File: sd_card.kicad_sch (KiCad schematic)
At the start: 3 parts

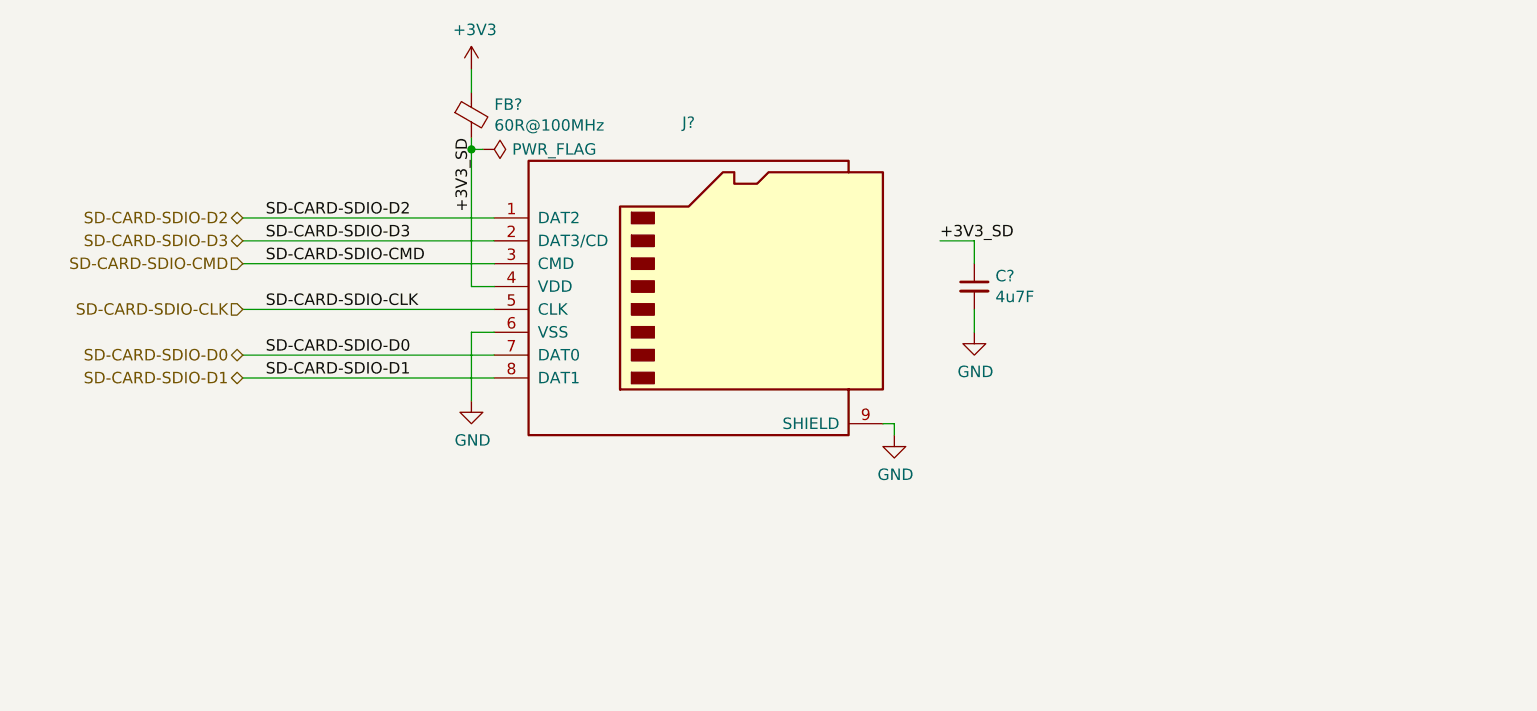
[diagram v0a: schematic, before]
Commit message: Refactor the mainboard
- Use smaller STM
- Use MPU-9250 as a motion sensor
- Connect some peripherals to the MCU
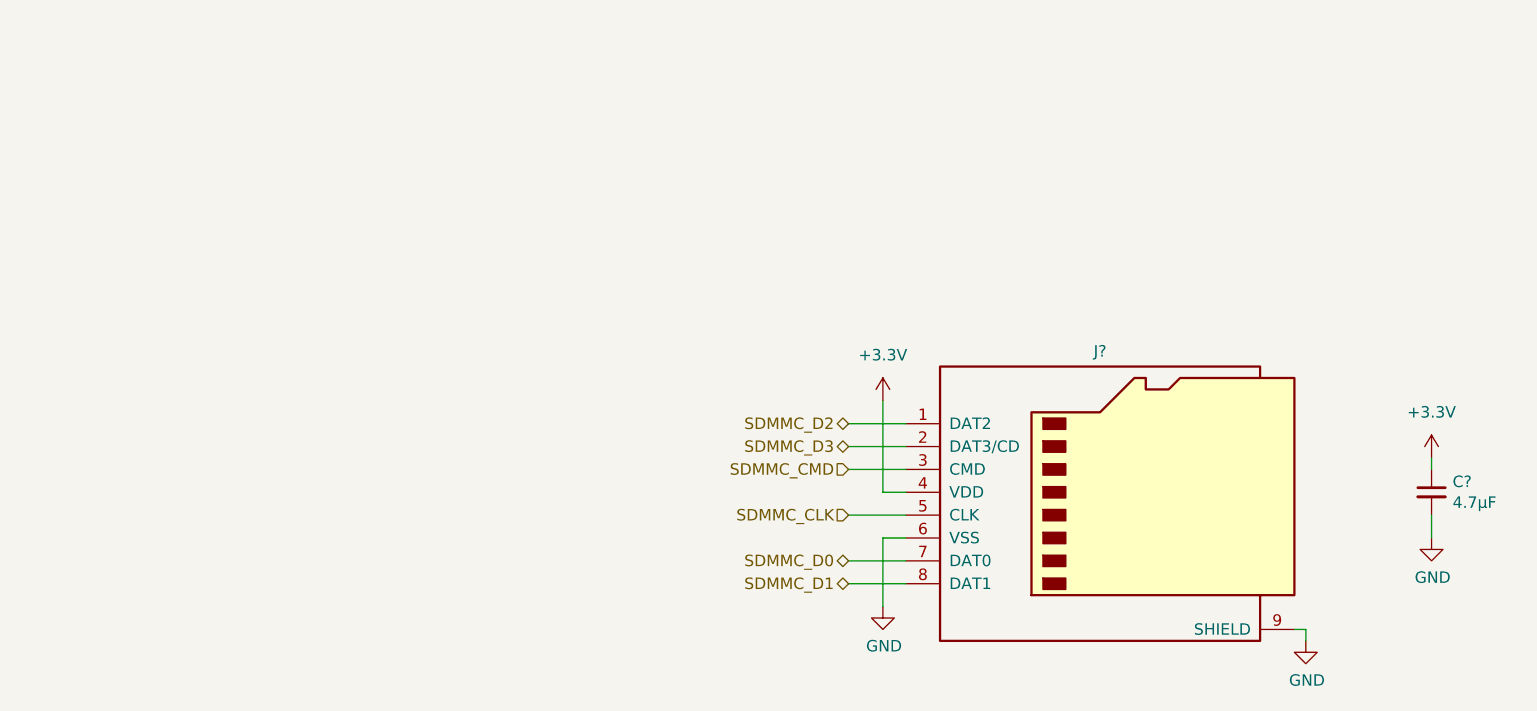
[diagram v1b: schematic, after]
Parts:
- removed FB?: 60R@100MHz, Inductor_SMD:L_0603_1608Metric, symbol Device:Ferrite_Bead_Small
- C?: value 4u7F -> 4.7μF
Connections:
- net +3V3_SD renamed +3.3V
- net SD-CARD-SDIO-CLK renamed SDMMC_CLK
- net SD-CARD-SDIO-CMD renamed SDMMC_CMD
- net SD-CARD-SDIO-D0 renamed SDMMC_D0
- net SD-CARD-SDIO-D1 renamed SDMMC_D1
- net SD-CARD-SDIO-D2 renamed SDMMC_D2
- net SD-CARD-SDIO-D3 renamed SDMMC_D3
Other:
- moved on the sheet: C?, J?

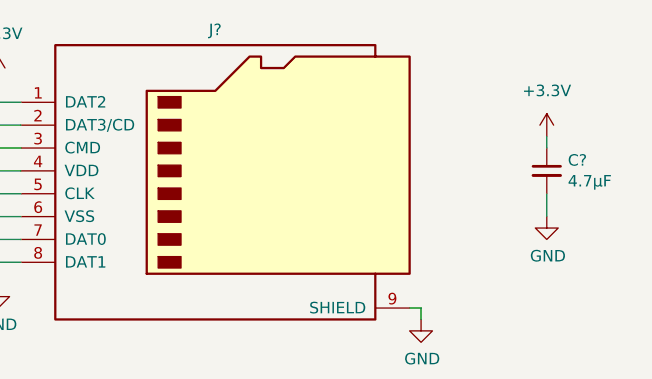
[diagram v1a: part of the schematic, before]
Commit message: Connect sensors to the MCU
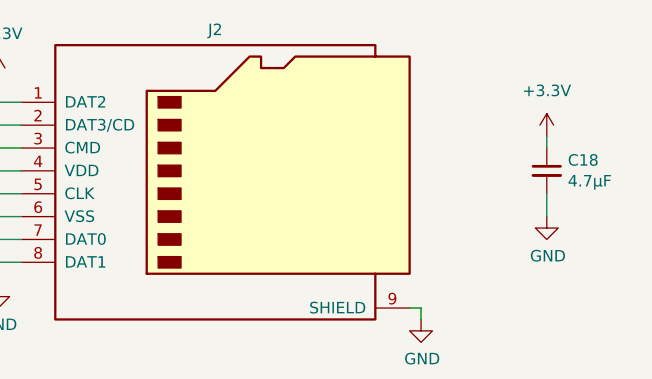
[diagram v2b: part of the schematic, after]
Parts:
- gave numbers to parts that had none: 2
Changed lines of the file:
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@@
 (kicad_sch (version 20211123) (generator eeschema)
   (paper "A4")
+  (title_block
+    (date "2022-12-16")
+    (rev "0.1.0")
+  )
   (wire (pts (xy 186.69 118.11) (xy 185.42 118.11))
     (stroke (width 0) (type default) (color 0 0 0 0))
@@
   (symbol (lib_id "Connector:Micro_SD_Card") (at 165.1 102.87 0) (unit 1)
     (in_bom yes) (on_board yes)
-    (property "Reference" "J?" (id 0) (at 163.83 87.1982 0))
+    (property "Reference" "J2" (id 0) (at 163.83 87.1982 0))
     (property "Value" "Micro_SD_Card" (id 1) (at 163.83 86.9696 0)
       (effects (font (size 1.27 1.27)) hide)
@@
   (symbol (lib_id "Device:C_Small") (at 200.66 102.87 0) (unit 1)
     (in_bom yes) (on_board yes)
-    (property "Reference" "C?" (id 0) (at 202.9968 101.7016 0)
+    (property "Reference" "C18" (id 0) (at 202.9968 101.7016 0)
       (effects (font (size 1.27 1.27)) (justify left))
     )
@@
   (symbol (lib_id "power:GND") (at 200.66 107.95 0) (unit 1)
     (in_bom yes) (on_board yes)
-    (property "Reference" "#PWR?" (id 0) (at 200.66 114.3 0)
+    (property "Reference" "#PWR0135" (id 0) (at 200.66 114.3 0)
       (effects (font (size 1.27 1.27)) hide)
     )
@@
   (symbol (lib_id "power:+3.3V") (at 200.66 99.06 0) (unit 1)
     (in_bom yes) (on_board yes) (fields_autoplaced)
-    (property "Reference" "#PWR?" (id 0) (at 200.66 102.87 0)
+    (property "Reference" "#PWR0134" (id 0) (at 200.66 102.87 0)
       (effects (font (size 1.27 1.27)) hide)
     )
@@
   (symbol (lib_id "power:+3.3V") (at 139.7 92.71 0) (unit 1)
     (in_bom yes) (on_board yes) (fields_autoplaced)
-    (property "Reference" "#PWR?" (id 0) (at 139.7 96.52 0)
+    (property "Reference" "#PWR0137" (id 0) (at 139.7 96.52 0)
       (effects (font (size 1.27 1.27)) hide)
     )
@@
   (symbol (lib_id "power:GND") (at 139.7 115.57 0) (unit 1)
     (in_bom yes) (on_board yes)
-    (property "Reference" "#PWR?" (id 0) (at 139.7 121.92 0)
+    (property "Reference" "#PWR0133" (id 0) (at 139.7 121.92 0)
       (effects (font (size 1.27 1.27)) hide)
     )
@@
   (symbol (lib_id "power:GND") (at 186.69 119.38 0) (unit 1)
     (in_bom yes) (on_board yes)
-    (property "Reference" "#PWR?" (id 0) (at 186.69 125.73 0)
+    (property "Reference" "#PWR0136" (id 0) (at 186.69 125.73 0)
       (effects (font (size 1.27 1.27)) hide)
     )

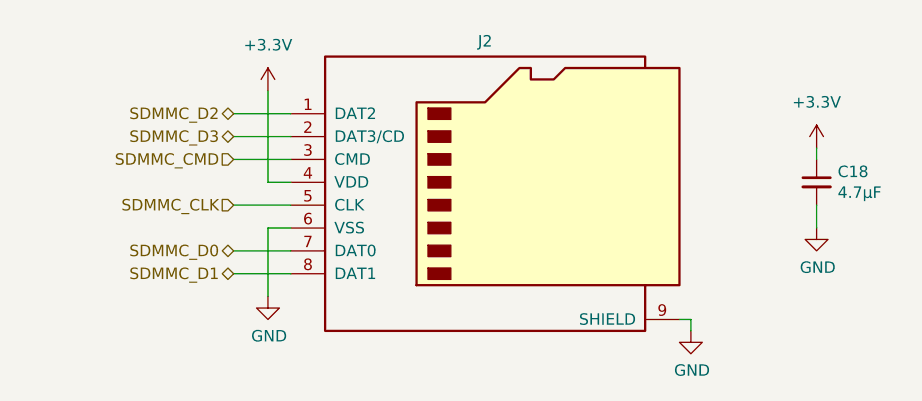
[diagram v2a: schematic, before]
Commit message: Improve the power section:
- add ADC circuit to measure battery level
- add 5V LDO regulator
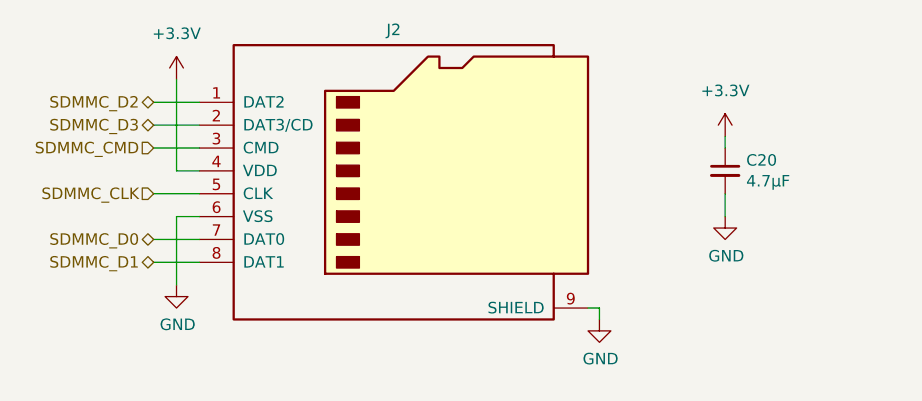
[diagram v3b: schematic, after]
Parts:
- renumbered C18 to C20
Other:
- title: (none) -> SD Card
- moved on the sheet: C20, J2
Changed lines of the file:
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@@
   (paper "A4")
   (title_block
-    (date "2022-12-16")
+    (title "SD Card")
+    (date "2022-12-17")
     (rev "0.1.0")
   )
-  (wire (pts (xy 186.69 118.11) (xy 185.42 118.11))
+  (wire (pts (xy 176.53 116.84) (xy 175.26 116.84))
     (stroke (width 0) (type default) (color 0 0 0 0))
   )
-  (wire (pts (xy 135.89 95.25) (xy 142.24 95.25))
+  (wire (pts (xy 127 93.98) (xy 132.08 93.98))
     (stroke (width 0) (type default) (color 0 0 0 0))
   )
-  (wire (pts (xy 142.24 113.03) (xy 135.89 113.03))
+  (wire (pts (xy 132.08 111.76) (xy 127 111.76))
     (stroke (width 0) (type default) (color 0 0 0 0))
   )
-  (wire (pts (xy 135.89 105.41) (xy 142.24 105.41))
+  (wire (pts (xy 127 104.14) (xy 132.08 104.14))
     (stroke (width 0) (type default) (color 0 0 0 0))
   )
-  (wire (pts (xy 139.7 107.95) (xy 142.24 107.95))
+  (wire (pts (xy 129.54 106.68) (xy 132.08 106.68))
     (stroke (width 0) (type default) (color 0 0 0 0))
   )
-  (wire (pts (xy 200.66 105.41) (xy 200.66 107.95))
+  (wire (pts (xy 190.5 104.14) (xy 190.5 106.68))
     (stroke (width 0) (type default) (color 0 0 0 0))
   )
-  (wire (pts (xy 186.69 119.38) (xy 186.69 118.11))
+  (wire (pts (xy 176.53 118.11) (xy 176.53 116.84))
     (stroke (width 0) (type default) (color 0 0 0 0))
   )
-  (wire (pts (xy 135.89 97.79) (xy 142.24 97.79))
+  (wire (pts (xy 127 96.52) (xy 132.08 96.52))
     (stroke (width 0) (type default) (color 0 0 0 0))
   )
-  (wire (pts (xy 135.89 110.49) (xy 142.24 110.49))
+  (wire (pts (xy 127 109.22) (xy 132.08 109.22))
     (stroke (width 0) (type default) (color 0 0 0 0))
   )
-  (wire (pts (xy 200.66 99.06) (xy 200.66 100.33))
+  (wire (pts (xy 190.5 97.79) (xy 190.5 99.06))
     (stroke (width 0) (type default) (color 0 0 0 0))
   )
-  (wire (pts (xy 142.24 102.87) (xy 139.7 102.87))
+  (wire (pts (xy 132.08 101.6) (xy 129.54 101.6))
     (stroke (width 0) (type default) (color 0 0 0 0))
   )
-  (wire (pts (xy 139.7 115.57) (xy 139.7 107.95))
+  (wire (pts (xy 129.54 114.3) (xy 129.54 106.68))
     (stroke (width 0) (type default) (color 0 0 0 0))
   )
-  (wire (pts (xy 139.7 92.71) (xy 139.7 102.87))
+  (wire (pts (xy 129.54 91.44) (xy 129.54 101.6))
     (stroke (width 0) (type default) (color 0 0 0 0))
   )
-  (wire (pts (xy 135.89 100.33) (xy 142.24 100.33))
+  (wire (pts (xy 127 99.06) (xy 132.08 99.06))
     (stroke (width 0) (type default) (color 0 0 0 0))
   )
-  (hierarchical_label "SDMMC_D3" (shape bidirectional) (at 135.89 97.79 180)
+  (hierarchical_label "SDMMC_D3" (shape bidirectional) (at 127 96.52 180)
     (effects (font (size 1.27 1.27)) (justify right))
   )
-  (hierarchical_label "SDMMC_D1" (shape bidirectional) (at 135.89 113.03 180)
+  (hierarchical_label "SDMMC_D1" (shape bidirectional) (at 127 111.76 180)
     (effects (font (size 1.27 1.27)) (justify right))
   )
-  (hierarchical_label "SDMMC_D2" (shape bidirectional) (at 135.89 95.25 180)
+  (hierarchical_label "SDMMC_D2" (shape bidirectional) (at 127 93.98 180)
     (effects (font (size 1.27 1.27)) (justify right))
   )
-  (hierarchical_label "SDMMC_D0" (shape bidirectional) (at 135.89 110.49 180)
+  (hierarchical_label "SDMMC_D0" (shape bidirectional) (at 127 109.22 180)
     (effects (font (size 1.27 1.27)) (justify right))
   )
-  (hierarchical_label "SDMMC_CLK" (shape input) (at 135.89 105.41 180)
+  (hierarchical_label "SDMMC_CLK" (shape input) (at 127 104.14 180)
     (effects (font (size 1.27 1.27)) (justify right))
   )
-  (hierarchical_label "SDMMC_CMD" (shape input) (at 135.89 100.33 180)
+  (hierarchical_label "SDMMC_CMD" (shape input) (at 127 99.06 180)
     (effects (font (size 1.27 1.27)) (justify right))
   )
-  (symbol (lib_id "Connector:Micro_SD_Card") (at 165.1 102.87 0) (unit 1)
+  (symbol (lib_id "Connector:Micro_SD_Card") (at 154.94 101.6 0) (unit 1)
     (in_bom yes) (on_board yes)
-    (property "Reference" "J2" (id 0) (at 163.83 87.1982 0))
-    (property "Value" "Micro_SD_Card" (id 1) (at 163.83 86.9696 0)
+    (property "Reference" "J2" (id 0) (at 153.67 85.9282 0))
+    (property "Value" "Micro_SD_Card" (id 1) (at 153.67 85.6996 0)
       (effects (font (size 1.27 1.27)) hide)
     )
-    (property "Footprint" "PUTM_Kicad_FOOTPRINTS:112K-TAA0-RA1" (id 2) (at 194.31 95.25 0)
+    (property "Footprint" "PUTM_Kicad_FOOTPRINTS:112K-TAA0-RA1" (id 2) (at 184.15 93.98 0)
       (effects (font (size 1.27 1.27)) hide)
     )
-    (property "Datasheet" "https://www.tme.eu/Document/c3b9a7ded342d5553aff6a91c42e4fab/112K-TAA0-RA1.pdf" (id 3) (at 165.1 102.87 0)
+    (property "Datasheet" "https://www.tme.eu/Document/c3b9a7ded342d5553aff6a91c42e4fab/112K-TAA0-RA1.pdf" (id 3) (at 154.94 101.6 0)
       (effects (font (size 1.27 1.27)) hide)
     )
@@
     (pin "9")
   )
-  (symbol (lib_id "Device:C_Small") (at 200.66 102.87 0) (unit 1)
+  (symbol (lib_id "Device:C_Small") (at 190.5 101.6 0) (unit 1)
     (in_bom yes) (on_board yes)
-    (property "Reference" "C18" (id 0) (at 202.9968 101.7016 0)
+    (property "Reference" "C20" (id 0) (at 192.8368 100.4316 0)
       (effects (font (size 1.27 1.27)) (justify left))
     )
-    (property "Value" "4.7μF" (id 1) (at 202.9968 104.013 0)
+    (property "Value" "4.7μF" (id 1) (at 192.8368 102.743 0)
       (effects (font (size 1.27 1.27)) (justify left))
     )
-    (property "Footprint" "Capacitor_SMD:C_0603_1608Metric" (id 2) (at 200.66 102.87 0)
+    (property "Footprint" "Capacitor_SMD:C_0603_1608Metric" (id 2) (at 190.5 101.6 0)
       (effects (font (size 1.27 1.27)) hide)
     )
-    (property "Datasheet" "~" (id 3) (at 200.66 102.87 0)
+    (property "Datasheet" "~" (id 3) (at 190.5 101.6 0)
       (effects (font (size 1.27 1.27)) hide)
     )
-    (property "LCSC" "C19666" (id 4) (at 200.66 102.87 0)
+    (property "LCSC" "C19666" (id 4) (at 190.5 101.6 0)
       (effects (font (size 1.27 1.27)) hide)
     )
@@
     (pin "2")
   )
-  (symbol (lib_id "power:GND") (at 200.66 107.95 0) (unit 1)
+  (symbol (lib_id "power:GND") (at 190.5 106.68 0) (unit 1)
     (in_bom yes) (on_board yes)
-    (property "Reference" "#PWR0135" (id 0) (at 200.66 114.3 0)
+    (property "Reference" "#PWR040" (id 0) (at 190.5 113.03 0)
       (effects (font (size 1.27 1.27)) hide)
     )
-    (property "Value" "GND" (id 1) (at 200.787 112.3442 0))
-    (property "Footprint" "" (id 2) (at 200.66 107.95 0)
+    (property "Value" "GND" (id 1) (at 190.627 111.0742 0))
+    (property "Footprint" "" (id 2) (at 190.5 106.68 0)
       (effects (font (size 1.27 1.27)) hide)
     )
-    (property "Datasheet" "" (id 3) (at 200.66 107.95 0)
+    (property "Datasheet" "" (id 3) (at 190.5 106.68 0)
       (effects (font (size 1.27 1.27)) hide)
     )
     (pin "1")
   )
-  (symbol (lib_id "power:+3.3V") (at 200.66 99.06 0) (unit 1)
+  (symbol (lib_id "power:+3.3V") (at 190.5 97.79 0) (unit 1)
     (in_bom yes) (on_board yes) (fields_autoplaced)
-    (property "Reference" "#PWR0134" (id 0) (at 200.66 102.87 0)
+    (property "Reference" "#PWR039" (id 0) (at 190.5 101.6 0)
       (effects (font (size 1.27 1.27)) hide)
     )
-    (property "Value" "+3.3V" (id 1) (at 200.66 93.98 0))
-    (property "Footprint" "" (id 2) (at 200.66 99.06 0)
+    (property "Value" "+3.3V" (id 1) (at 190.5 92.71 0))
+    (property "Footprint" "" (id 2) (at 190.5 97.79 0)
       (effects (font (size 1.27 1.27)) hide)
     )
-    (property "Datasheet" "" (id 3) (at 200.66 99.06 0)
+    (property "Datasheet" "" (id 3) (at 190.5 97.79 0)
       (effects (font (size 1.27 1.27)) hide)
     )
     (pin "1")
   )
-  (symbol (lib_id "power:+3.3V") (at 139.7 92.71 0) (unit 1)
+  (symbol (lib_id "power:+3.3V") (at 129.54 91.44 0) (unit 1)
     (in_bom yes) (on_board yes) (fields_autoplaced)
-    (property "Reference" "#PWR0137" (id 0) (at 139.7 96.52 0)
+    (property "Reference" "#PWR038" (id 0) (at 129.54 95.25 0)
       (effects (font (size 1.27 1.27)) hide)
     )
-    (property "Value" "+3.3V" (id 1) (at 139.7 87.63 0))
-    (property "Footprint" "" (id 2) (at 139.7 92.71 0)
+    (property "Value" "+3.3V" (id 1) (at 129.54 86.36 0))
+    (property "Footprint" "" (id 2) (at 129.54 91.44 0)
       (effects (font (size 1.27 1.27)) hide)
     )
-    (property "Datasheet" "" (id 3) (at 139.7 92.71 0)
+    (property "Datasheet" "" (id 3) (at 129.54 91.44 0)
       (effects (font (size 1.27 1.27)) hide)
     )
     (pin "1")
   )
-  (symbol (lib_id "power:GND") (at 139.7 115.57 0) (unit 1)
+  (symbol (lib_id "power:GND") (at 129.54 114.3 0) (unit 1)
     (in_bom yes) (on_board yes)
-    (property "Reference" "#PWR0133" (id 0) (at 139.7 121.92 0)
+    (property "Reference" "#PWR041" (id 0) (at 129.54 120.65 0)
       (effects (font (size 1.27 1.27)) hide)
     )
-    (property "Value" "GND" (id 1) (at 139.827 119.9642 0))
-    (property "Footprint" "" (id 2) (at 139.7 115.57 0)
+    (property "Value" "GND" (id 1) (at 129.667 118.6942 0))
+    (property "Footprint" "" (id 2) (at 129.54 114.3 0)
       (effects (font (size 1.27 1.27)) hide)
     )
-    (property "Datasheet" "" (id 3) (at 139.7 115.57 0)
+    (property "Datasheet" "" (id 3) (at 129.54 114.3 0)
       (effects (font (size 1.27 1.27)) hide)
     )
     (pin "1")
   )
-  (symbol (lib_id "power:GND") (at 186.69 119.38 0) (unit 1)
+  (symbol (lib_id "power:GND") (at 176.53 118.11 0) (unit 1)
     (in_bom yes) (on_board yes)
-    (property "Reference" "#PWR0136" (id 0) (at 186.69 125.73 0)
+    (property "Reference" "#PWR042" (id 0) (at 176.53 124.46 0)
       (effects (font (size 1.27 1.27)) hide)
     )
-    (property "Value" "GND" (id 1) (at 186.817 123.7742 0))
-    (property "Footprint" "" (id 2) (at 186.69 119.38 0)
+    (property "Value" "GND" (id 1) (at 176.657 122.5042 0))
+    (property "Footprint" "" (id 2) (at 176.53 118.11 0)
       (effects (font (size 1.27 1.27)) hide)
     )
-    (property "Datasheet" "" (id 3) (at 186.69 119.38 0)
+    (property "Datasheet" "" (id 3) (at 176.53 118.11 0)
       (effects (font (size 1.27 1.27)) hide)
     )
